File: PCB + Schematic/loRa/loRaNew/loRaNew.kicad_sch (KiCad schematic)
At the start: 12 parts, among them J1 Left, J2 Right, J3 GPS, J4 MPU-9250, J7 OLED, SW1 SW_SPDT, U1 ESP32-DEVKIT-V1

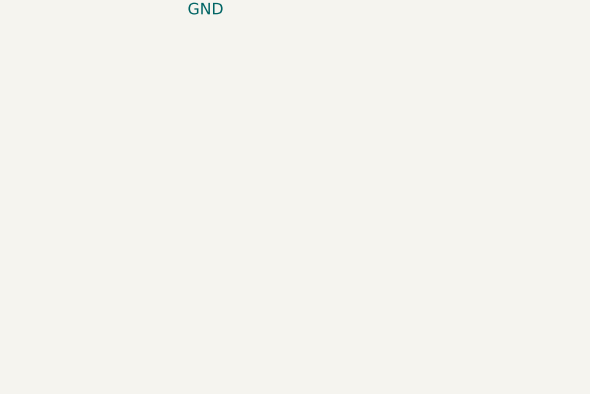
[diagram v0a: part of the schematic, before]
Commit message: LoRa PCB
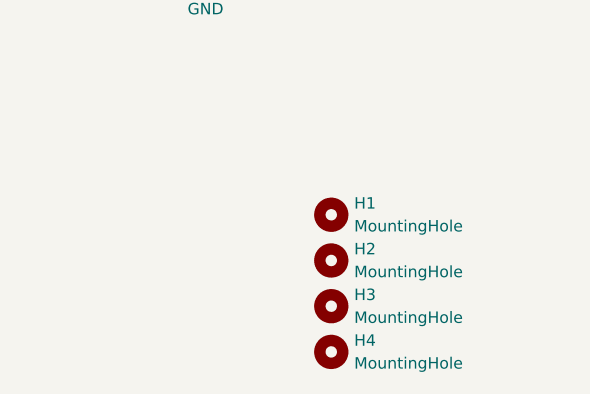
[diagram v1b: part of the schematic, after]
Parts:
- added H1, H2, H3, H4: MountingHole, MountingHole:MountingHole_3.2mm_M3, symbol Mechanical:MountingHole
